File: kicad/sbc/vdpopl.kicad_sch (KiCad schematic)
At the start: 23 parts, among them U2 V9958, U3 DRAM_64KX4, U4 DRAM_64KX4, U5 DRAM_64KX4, U6 DRAM_64KX4, U7 DRAM_64KX4, U8 YM3812, U9 DRAM_64KX4, Y1 21,443Mhz

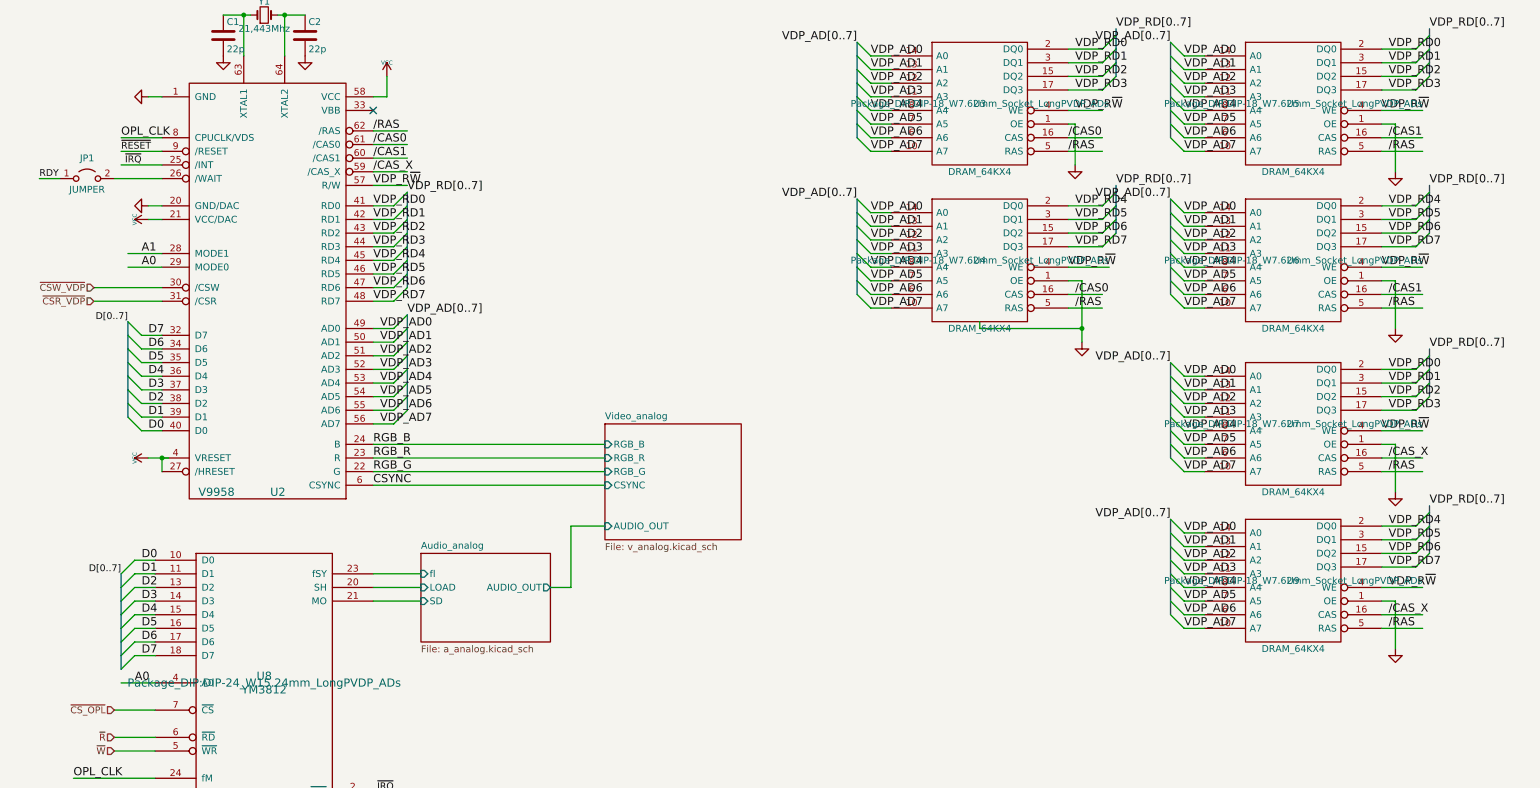
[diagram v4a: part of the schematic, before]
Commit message: erc cleanup
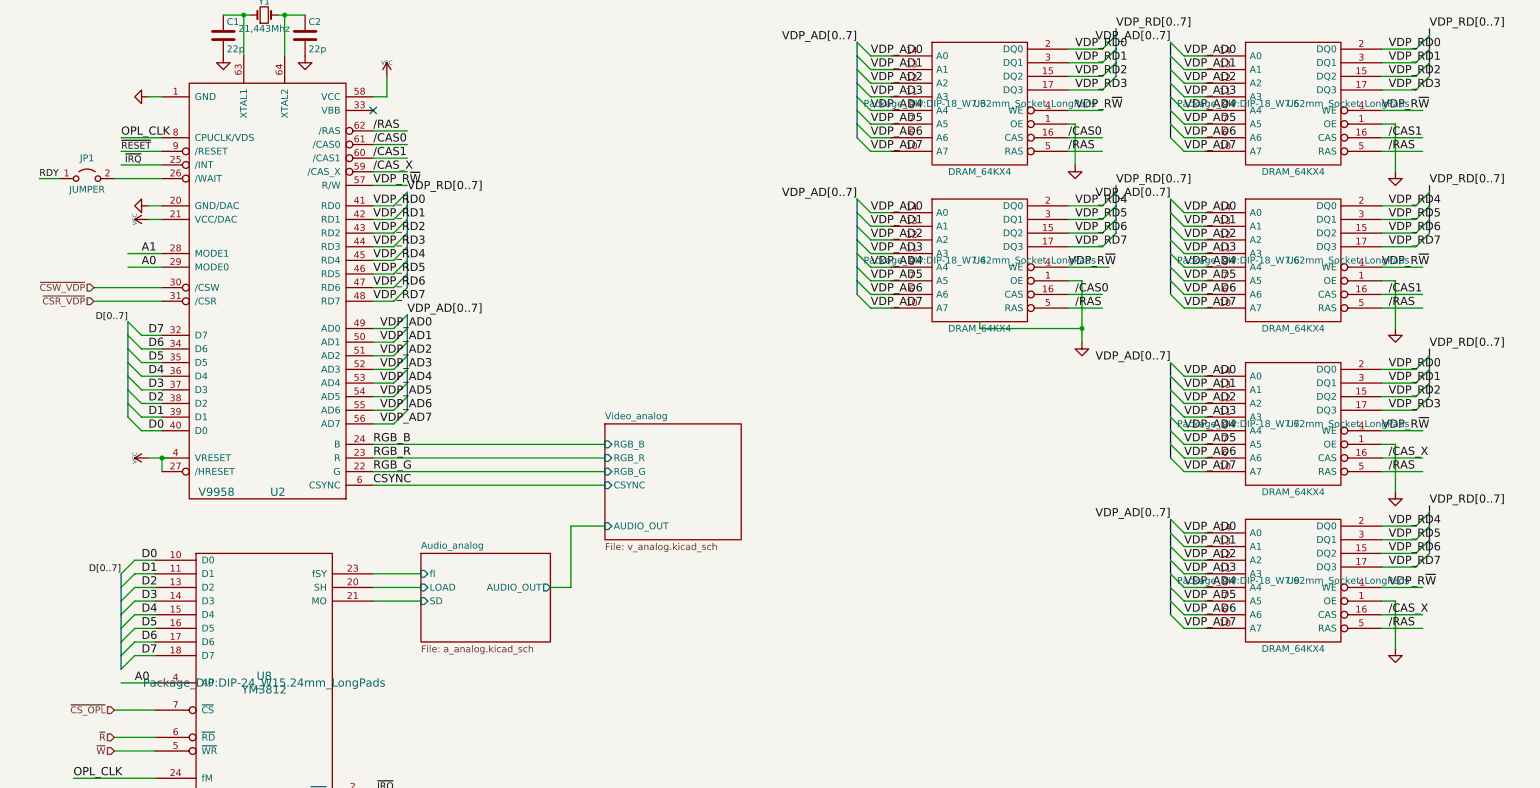
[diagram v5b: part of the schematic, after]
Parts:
- U3, U4, U5, U6, U7, U9: footprint Package_DIP:DIP-18_W7.62mm_Socket_LongPVDP_ADs -> Package_DIP:DIP-18_W7.62mm_Socket_LongPads
- U8: footprint Package_DIP:DIP-24_W15.24mm_LongPVDP_ADs -> Package_DIP:DIP-24_W15.24mm_LongPads
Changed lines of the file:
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@@
       (effects (font (size 1.27 1.27)))
     )
-    (property "Footprint" "Package_DIP:DIP-18_W7.62mm_Socket_LongPVDP_ADs" (at 252.73 123.19 0)
+    (property "Footprint" "Package_DIP:DIP-18_W7.62mm_Socket_LongPads" (at 252.73 123.19 0)
       (effects (font (size 1.27 1.27)))
     )
@@
       (effects (font (size 1.524 1.524)))
     )
-    (property "Footprint" "Package_DIP:DIP-24_W15.24mm_LongPVDP_ADs" (at 60.96 142.24 0)
+    (property "Footprint" "Package_DIP:DIP-24_W15.24mm_LongPads" (at 60.96 142.24 0)
       (effects (font (size 1.524 1.524)))
     )
@@
       (effects (font (size 1.27 1.27)))
     )
-    (property "Footprint" "Package_DIP:DIP-18_W7.62mm_Socket_LongPVDP_ADs" (at 194.31 34.29 0)
+    (property "Footprint" "Package_DIP:DIP-18_W7.62mm_Socket_LongPads" (at 194.31 34.29 0)
       (effects (font (size 1.27 1.27)))
     )
@@
       (effects (font (size 1.27 1.27)))
     )
-    (property "Footprint" "Package_DIP:DIP-18_W7.62mm_Socket_LongPVDP_ADs" (at 252.73 63.5 0)
+    (property "Footprint" "Package_DIP:DIP-18_W7.62mm_Socket_LongPads" (at 252.73 63.5 0)
       (effects (font (size 1.27 1.27)))
     )
@@
       (effects (font (size 1.27 1.27)))
     )
-    (property "Footprint" "Package_DIP:DIP-18_W7.62mm_Socket_LongPVDP_ADs" (at 252.73 93.98 0)
+    (property "Footprint" "Package_DIP:DIP-18_W7.62mm_Socket_LongPads" (at 252.73 93.98 0)
       (effects (font (size 1.27 1.27)))
     )
@@
       (effects (font (size 1.27 1.27)))
     )
-    (property "Footprint" "Package_DIP:DIP-18_W7.62mm_Socket_LongPVDP_ADs" (at 194.31 63.5 0)
+    (property "Footprint" "Package_DIP:DIP-18_W7.62mm_Socket_LongPads" (at 194.31 63.5 0)
       (effects (font (size 1.27 1.27)))
     )
@@
       (effects (font (size 1.27 1.27)))
     )
-    (property "Footprint" "Package_DIP:DIP-18_W7.62mm_Socket_LongPVDP_ADs" (at 252.73 34.29 0)
-      (effects (font (size 1.27 1.27)))
-    )
+    (property "Footprint" "Package_DIP:DIP-18_W7.62mm_Socket_LongPads" (at 252.73 34.29 0)
+      (effects (font (size 1.27 1.27)))
+    )

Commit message: DRC hell II
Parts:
- removed C8: 100n, Capacitor_SMD:C_1206_3216Metric_Pad1.33x1.80mm_HandSolder, symbol Device:C
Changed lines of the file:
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@@
   (junction (at 135.89 189.23) (diameter 0) (color 0 0 0 0)
   )
-  (junction (at 120.65 181.61) (diameter 0) (color 0 0 0 0)
-  )
   (junction (at 82.55 189.23) (diameter 0) (color 0 0 0 0)
   )
-  (junction (at 120.65 189.23) (diameter 0) (color 0 0 0 0)
-  )
   (junction (at 113.03 181.61) (diameter 0) (color 0 0 0 0)
   )
@@
     (stroke (width 0) (type default))
   )
-  (wire (pts (xy 120.65 189.23) (xy 128.27 189.23))
-    (stroke (width 0) (type default))
-  )
   (bus (pts (xy 219.71 53.34) (xy 219.71 55.88))
     (stroke (width 0) (type default))
@@
     (stroke (width 0) (type default))
   )
-  (wire (pts (xy 113.03 181.61) (xy 120.65 181.61))
+  (wire (pts (xy 113.03 181.61) (xy 128.27 181.61))
     (stroke (width 0) (type default))
   )
@@
     (stroke (width 0) (type default))
   )
-  (wire (pts (xy 113.03 189.23) (xy 120.65 189.23))
+  (wire (pts (xy 113.03 189.23) (xy 128.27 189.23))
     (stroke (width 0) (type default))
   )
@@
     (stroke (width 0) (type default))
   )
-  (wire (pts (xy 120.65 181.61) (xy 128.27 181.61))
-    (stroke (width 0) (type default))
-  )
   (bus (pts (xy 229.87 57.15) (xy 229.87 59.69))
     (stroke (width 0) (type default))
@@
         )
       )
-    )
-  )
-  (symbol (lib_id "Device:C") (at 120.65 185.42 0) (unit 1)
-    (in_bom yes) (on_board yes) (dnp no)
-    (property "Reference" "C8" (at 121.285 182.88 0)
-      (effects (font (size 1.27 1.27)) (justify left))
-    )
-    (property "Value" "100n" (at 121.285 187.96 0)
-      (effects (font (size 1.27 1.27)) (justify left))
-    )
-    (property "Footprint" "Capacitor_SMD:C_1206_3216Metric_Pad1.33x1.80mm_HandSolder" (at 121.6152 189.23 0)
-      (effects (font (size 1.27 1.27)) hide)
-    )
-    (property "Datasheet" "~" (at 120.65 185.42 0)
-      (effects (font (size 1.27 1.27)) hide)
-    )
-    (pin "1")
-    (pin "2")
-    (instances
-      (project "v9958"
-        (path "/8677aa04-d5f3-4ab1-a2c2-991cda76ac9e"
-          (reference "C8") (unit 1)
-        )
-      )
-      (project "sbc"
-        (path "/896d5dab-44ec-47d0-8232-7ef57773545e/28a4b651-8375-4e62-9061-4149cd570bf0"
-          (reference "C31") (unit 1)
-        )
-      )

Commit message: vdp xtal capacitor footprints THT
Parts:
- C1, C2: footprint Capacitor_SMD:C_1206_3216Metric_Pad1.33x1.80mm_HandSolder -> Capacitor_THT:C_Disc_D3.0mm_W2.0mm_P2.50mm
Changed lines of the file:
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@@
       (effects (font (size 1.27 1.27)) (justify left))
     )
-    (property "Footprint" "Capacitor_SMD:C_1206_3216Metric_Pad1.33x1.80mm_HandSolder" (at 54.3052 25.4 0)
+    (property "Footprint" "Capacitor_THT:C_Disc_D3.0mm_W2.0mm_P2.50mm" (at 54.3052 25.4 0)
       (effects (font (size 1.27 1.27)) hide)
     )
@@
       (effects (font (size 1.27 1.27)) (justify left))
     )
-    (property "Footprint" "Capacitor_SMD:C_1206_3216Metric_Pad1.33x1.80mm_HandSolder" (at 69.5452 25.4 0)
-      (effects (font (size 1.27 1.27)) hide)
-    )
+    (property "Footprint" "Capacitor_THT:C_Disc_D3.0mm_W2.0mm_P2.50mm" (at 69.5452 25.4 0)
+      (effects (font (size 1.27 1.27)) hide)
+    )
